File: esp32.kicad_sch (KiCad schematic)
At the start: 21 parts, among them J2 TC2030-IDC, J3 Conn_01x04, J4 Conn_01x06, J5 USB_C_Receptacle_USB2.0, SW1 GT-TC029B-H025-L1N, SW2 GT-TC029B-H025-L1N, U3 RT9080-33GJ5, U4 ESP32-S3-WROOM-1

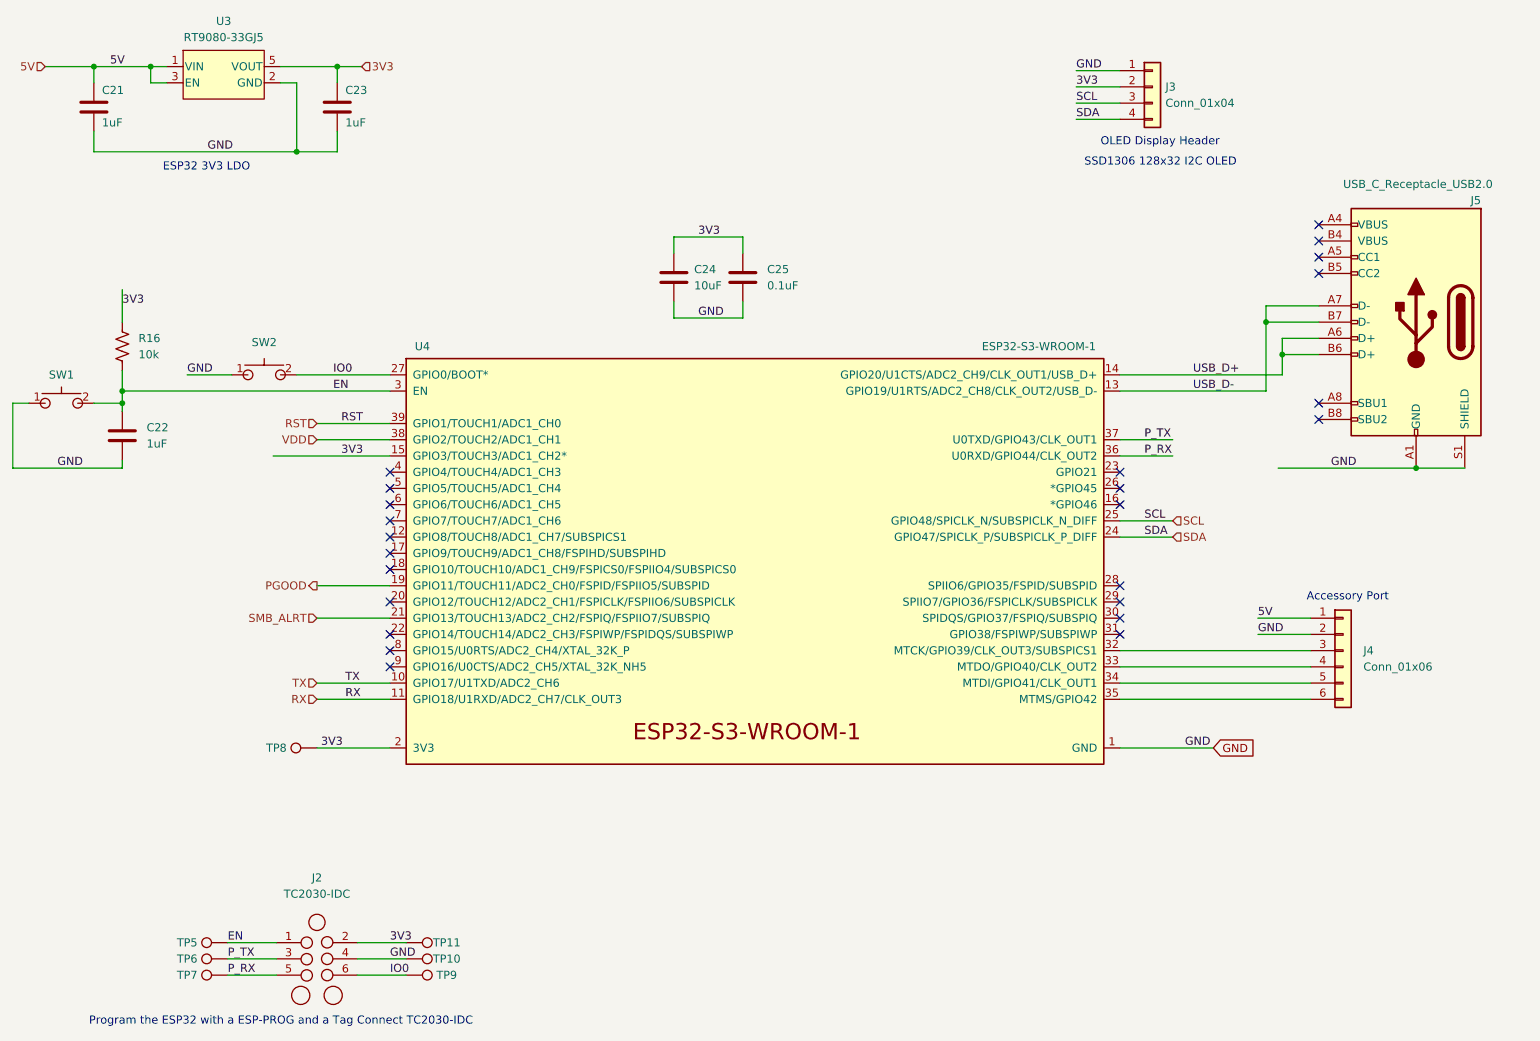
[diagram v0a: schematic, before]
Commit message: use global GND level provided by default with KiCad and remove custom global GND
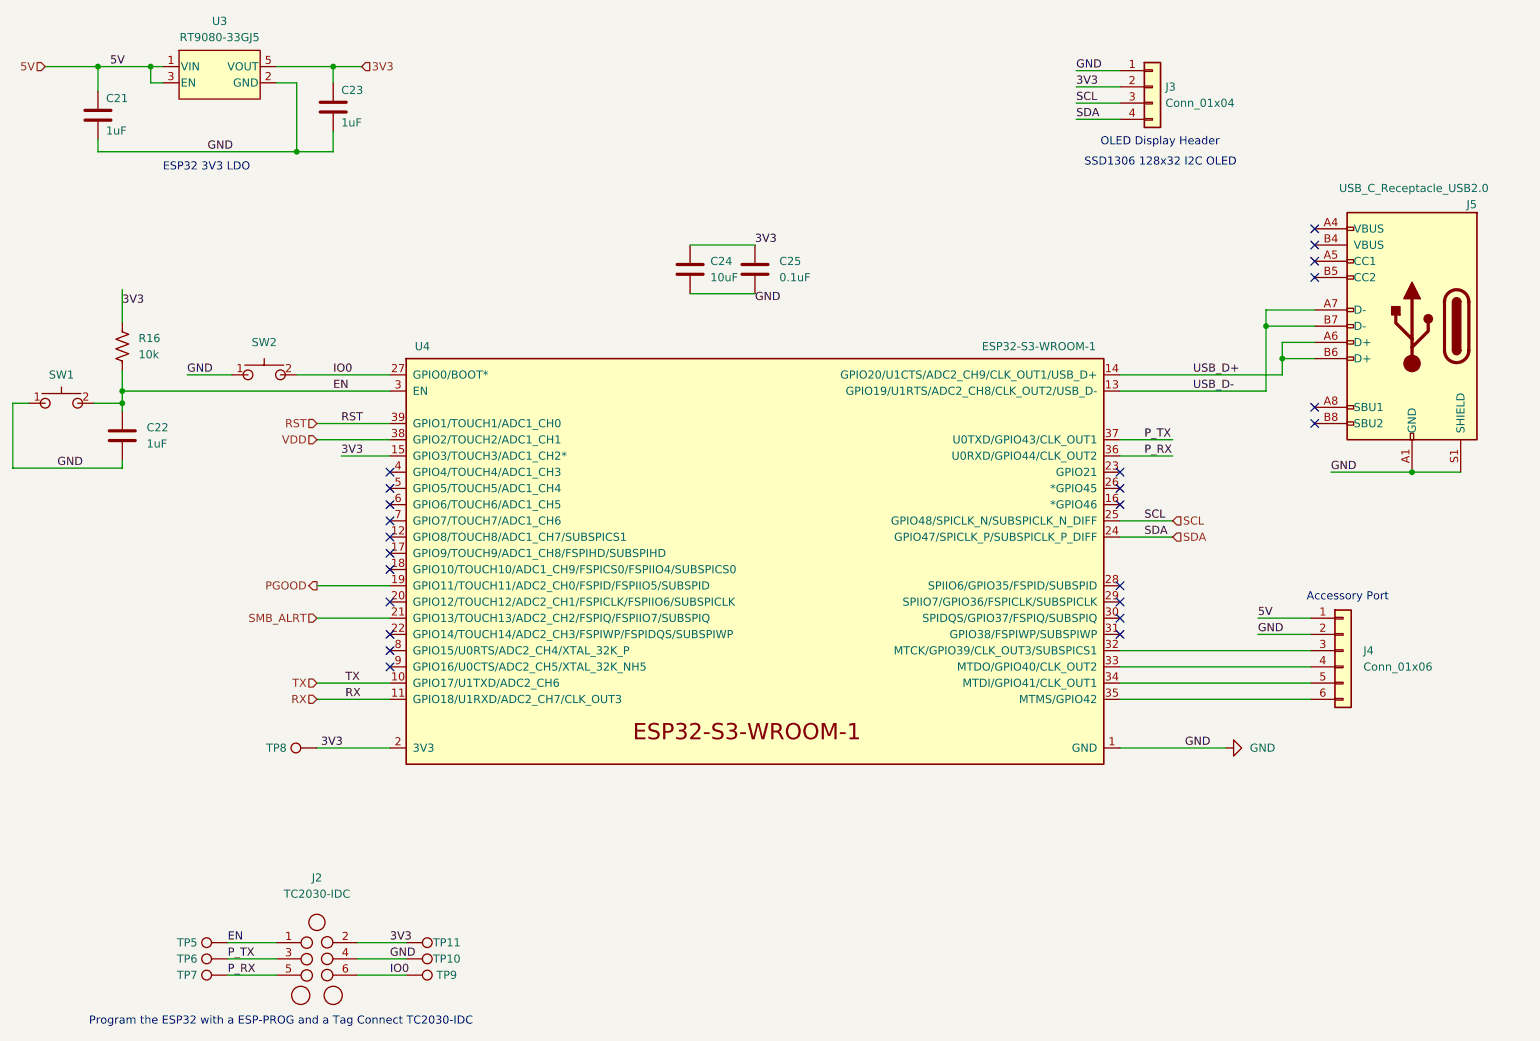
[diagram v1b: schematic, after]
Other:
- moved on the sheet: C21, C23, C24, C25, J5, U3
